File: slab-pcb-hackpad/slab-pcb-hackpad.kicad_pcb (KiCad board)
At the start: 2 copper layers, 120 x 95 mm, 108 parts, among them J1 MagnetR, J2 MagnetL, J3 TRRS_R, J4 TRRS_L, J5 SSD1306, J6 Conn_01x06, Q1 MMBT3906, U1 Seeeduino Xiao rp2040, U2 PCA9555PW, U3 PCA9555PW, U4 PW14

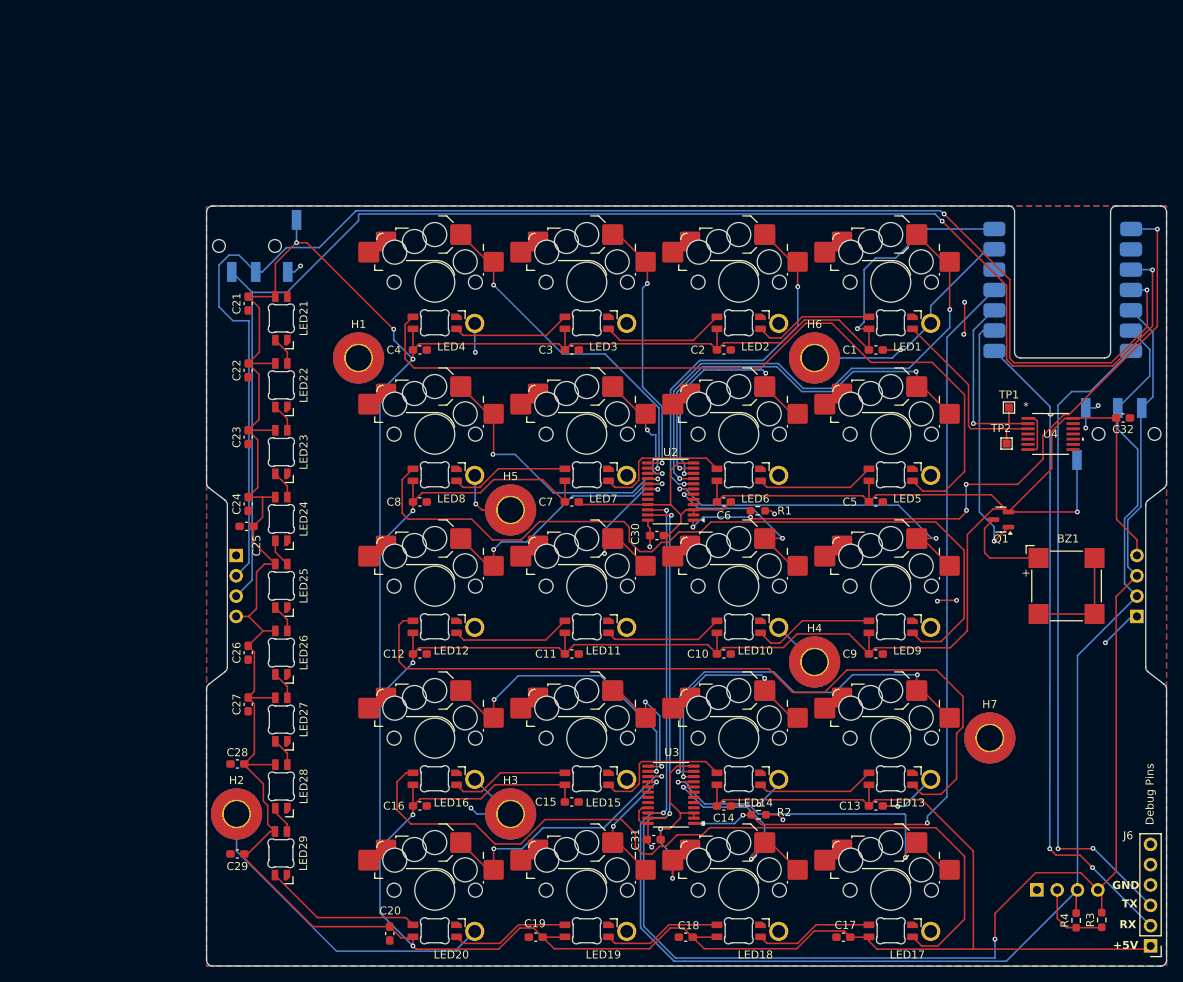
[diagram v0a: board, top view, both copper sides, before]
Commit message: fix: inconsistent design
all modules now share the same design - with updated footprints to
support both choc+mx PCB mounting holes.
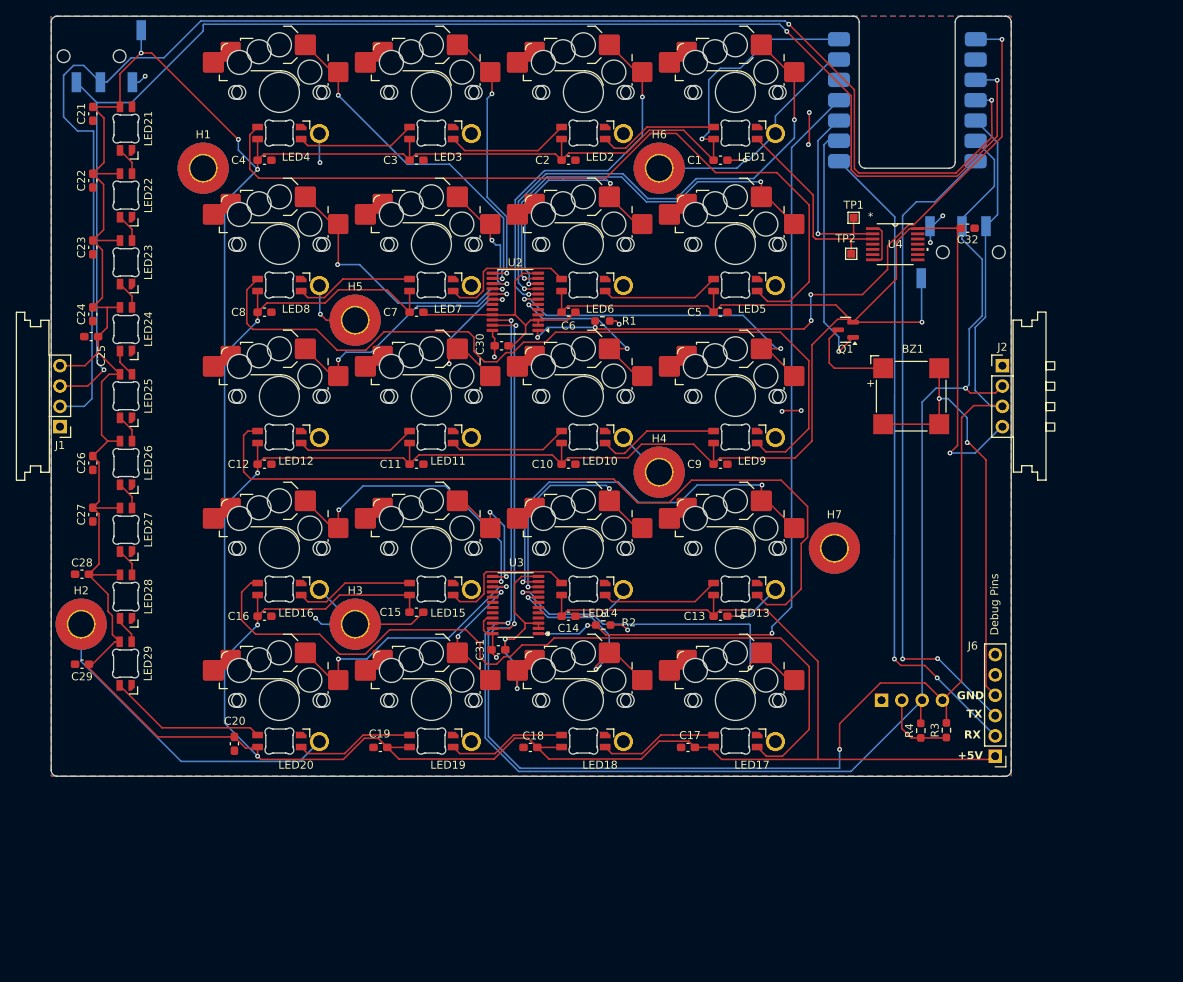
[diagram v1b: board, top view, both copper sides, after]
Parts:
- J1, J2: moved to F.Cu
- U4: value PW14 -> SN74AHCT125PWR
- moved J1 32.4 mm to (85.7, 93.8)
- moved C15 30.7 mm to (130.2, 120.8)
- moved C18 30.7 mm to (144.5, 137.7)
- moved C27 30.7 mm to (89.8, 108.6)
- moved C30 30.7 mm to (140.9, 87.5)
- moved H7 30.7 mm to (182.5, 112.8)
- moved LED29 30.7 mm to (93.9, 127.2)
- moved Q1 30.7 mm to (183.9, 85.5)
- moved R1 30.7 mm to (153.5, 84.4)
- moved R3 30.7 mm to (196.5, 135.5)
- moved REF** 30.7 mm to (195.0, 90.8)
- moved TP1 30.7 mm to (184.9, 71.5)
- moved U3 30.7 mm to (142.6, 119.9)
- moved C21 30.7 mm to (89.8, 58.5)
- moved C19 30.7 mm to (125.7, 137.7)
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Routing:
- net GND: track 206.1 -> 250.7 mm, vias 12 -> 13
- net VBUS: track 774.5 -> 796.9 mm, vias 9 -> 10
- net /I2C1_SCL: track 199.8 -> 205.9 mm, vias 2 -> 3
- net /I2C0_SCL: track 185.1 -> 190.5 mm
- net /I2C1_SDA: track 207.3 -> 212.2 mm
- net /I2C0_SDA: track 184.5 -> 185.9 mm, vias 2 -> 3
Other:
- outline, holes or cut-outs redrawn
